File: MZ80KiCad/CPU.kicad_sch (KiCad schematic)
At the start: 26 parts, among them Q6 2SC373, SW1 SW_Push, U1 Z80CPU, U24 74LS00, U31 74121, U35 74LS244, U36 74LS241, U37 74LS241, U4 74LS14, U44 74LS244, U45 74LS244

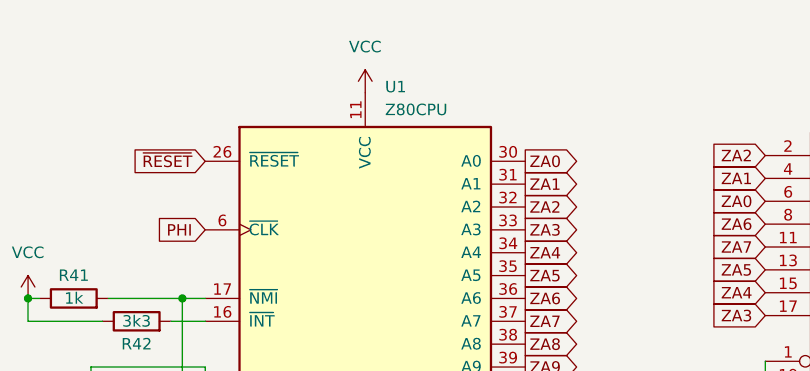
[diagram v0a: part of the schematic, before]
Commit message: fix U47 pin18 pin19
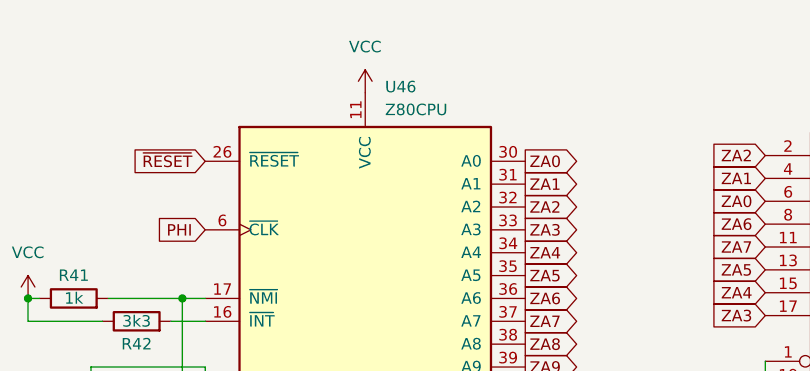
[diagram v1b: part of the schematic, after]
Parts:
- renumbered U1 to U46
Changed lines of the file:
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@@
   (symbol (lib_id "CPU:Z80CPU") (at 152.4 62.865 0) (unit 1)
     (in_bom yes) (on_board yes) (dnp no) (fields_autoplaced)
-    (property "Reference" "U1" (at 154.5941 24.13 0)
+    (property "Reference" "U46" (at 154.5941 24.13 0)
       (effects (font (size 1.27 1.27)) (justify left))
     )
@@
     (instances
       (project "MZ80"
-        (path "/4c07815a-c510-44da-af98-4d055fa8c080"
-          (reference "U1") (unit 1)
-        )
         (path "/4c07815a-c510-44da-af98-4d055fa8c080/bc1302d4-c004-470c-9bdf-6538c60fbf68"
           (reference "U46") (unit 1)

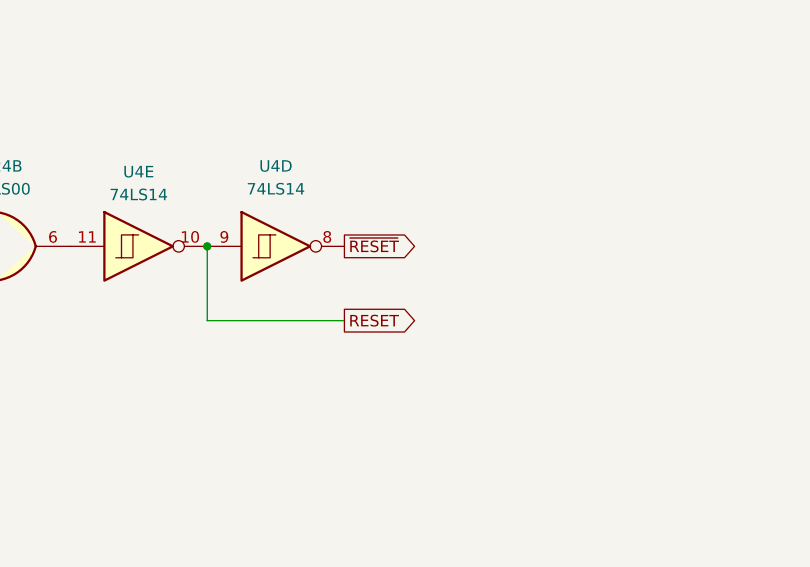
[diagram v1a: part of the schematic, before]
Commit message: fix RESET/*RESET
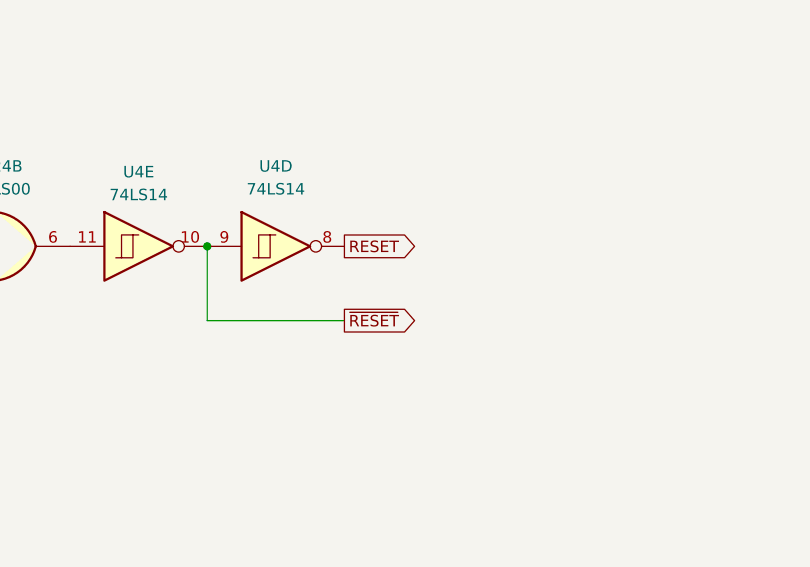
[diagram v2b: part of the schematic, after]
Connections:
- net RESET: now also U4.8; no longer U4.10, U4.9
- net ~{RESET}: now also U4.10, U4.9; no longer U4.8
